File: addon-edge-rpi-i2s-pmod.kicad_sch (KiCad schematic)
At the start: 34 parts, among them J1 PMOD1, J10 Conn_01x02, J11 Conn_01x01, J2 PMOD2, J3 PMOD3, J4 Conn_01x06, J5 Conn_01x06, J6 Conn_02x04_Top_Bottom, J7 Conn_01x03, J8 Conn_01x04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

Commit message: update 10/02/22 initial autorouting
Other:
- note added: "UART FPGA / RPi"
- note removed: "UART RPi"
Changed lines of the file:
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@@
     (effects (font (size 2.54 2.54)) (justify left bottom))
   )
-  (text "UART RPi" (at 22.86 140.97 0)
+  (text "UART FPGA / RPi" (at 20.32 140.97 0)
     (effects (font (size 1.27 1.27)) (justify left bottom))
   )

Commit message: rev 0.40
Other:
- note removed: "MIDI I2S SBC Pmod Edge Interface v0.1"
- note removed: "Somhic 09/02/22"
- note removed: "design rev. 0.38"
- company: Somhic -> Created by Hard Team Deca
- title: Addon Edge mt32-Pi Multicore  -> MIDI I2S SBC Pmod Edge Interface
- moved on the sheet: BUT1, BUT2, H1, H2, H3, H4, J1, J10, J11, J2, J3, J4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

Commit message: rev. 0.41
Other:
- note added: "Central +5V"
- note added: "DOUBLE PMOD 1,2"
- note added: "PMOD 3 (SPI+UART)"
- note removed: "Double Pmod +5V"
- note removed: "PMOD 3 Multicore"
- note removed: "PMODS 1,2"
- company: Created by Hard Team Deca -> Hard Team Deca
- moved on the sheet: BUT1, BUT2, H1, H2, H3, H4, J1, J10, J11, J2, J3, J4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

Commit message: 0.42
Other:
- note added: "EXPOSAR 8 PINS SRAM I 2 PINS I2C"

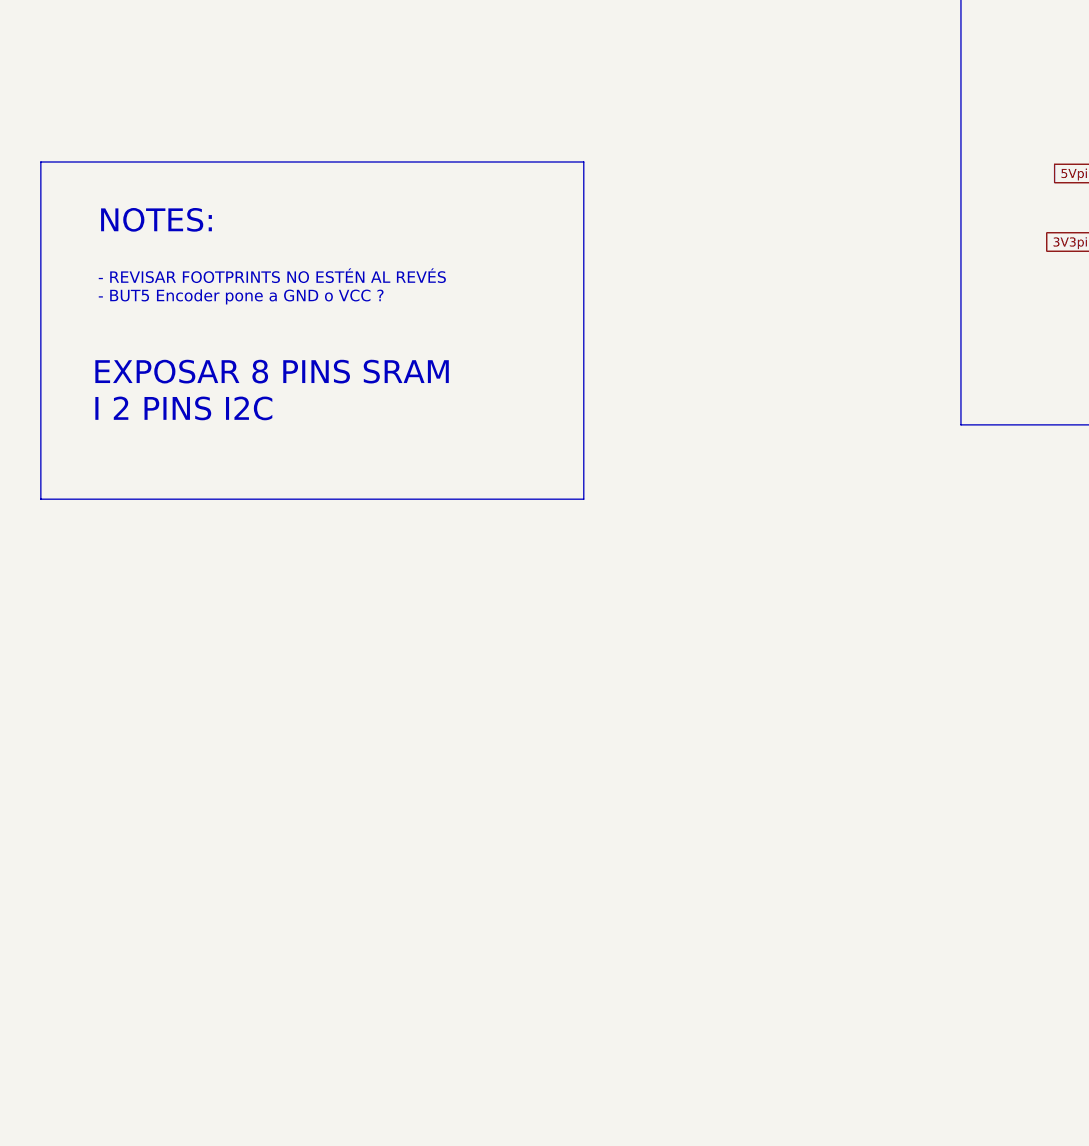
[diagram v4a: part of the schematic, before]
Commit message: modified jumper spacing for allowing switches
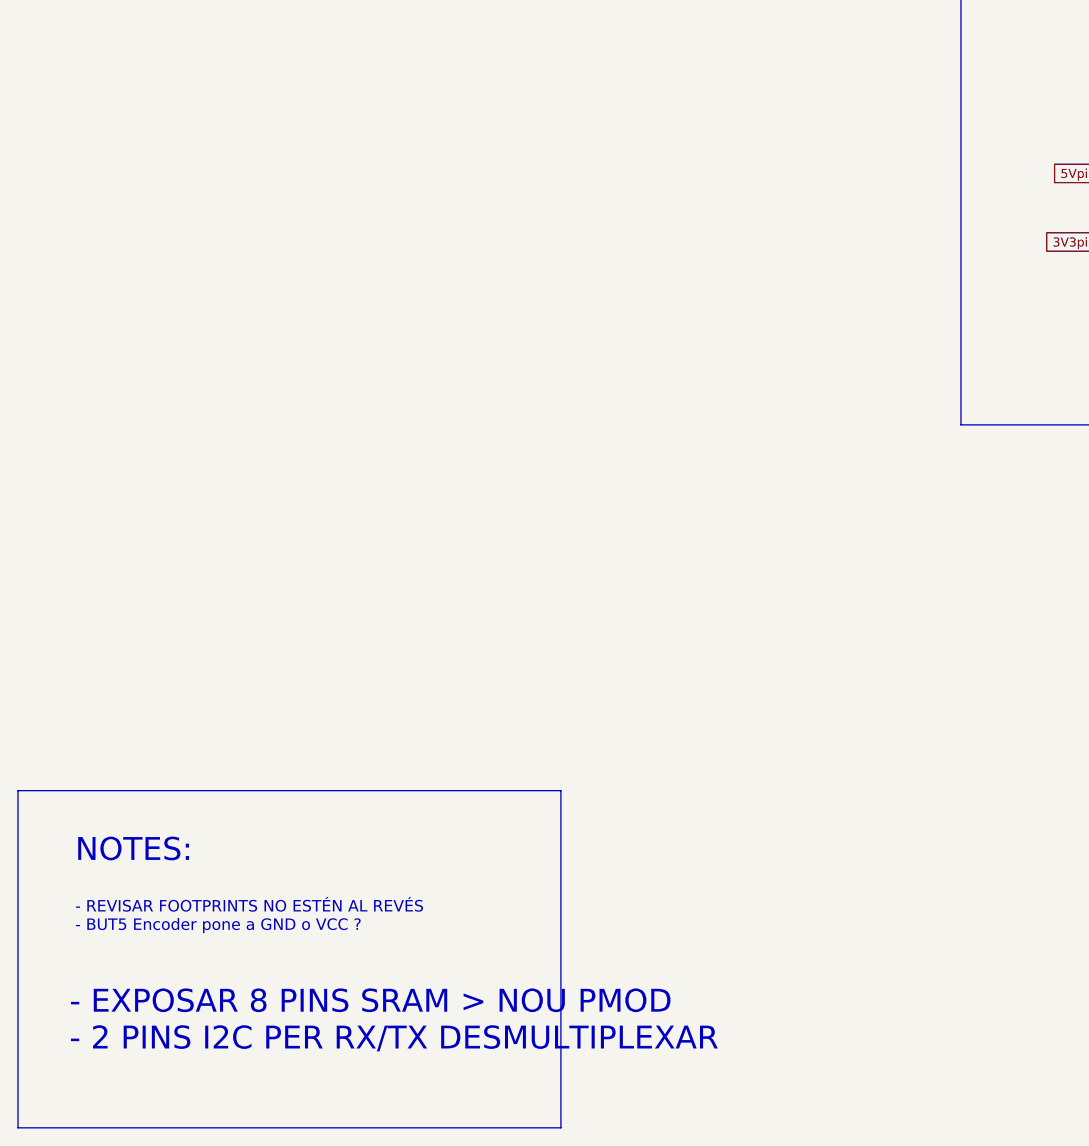
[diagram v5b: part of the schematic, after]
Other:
- note added: "- EXPOSAR 8 PINS SRAM > NOU PMOD - 2 PINS I2C PER RX/TX DESMULTIPLEXAR"
- note removed: "EXPOSAR 8 PINS SRAM I 2 PINS I2C"
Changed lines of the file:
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@@
     (stroke (width 0) (type default) (color 0 0 0 0))
   )
-  (polyline (pts (xy -3.81 253.365) (xy -64.135 253.365))
+  (polyline (pts (xy -6.35 323.215) (xy -66.675 323.215))
     (stroke (width 0) (type default) (color 0 0 0 0))
   )
@@
     (stroke (width 0) (type default) (color 0 0 0 0))
   )
-  (polyline (pts (xy -3.81 215.9) (xy -3.81 253.365))
+  (polyline (pts (xy -6.35 285.75) (xy -6.35 323.215))
     (stroke (width 0) (type default) (color 0 0 0 0))
   )
@@
     (stroke (width 0) (type default) (color 0 0 0 0))
   )
-  (polyline (pts (xy -64.135 215.9) (xy -3.81 215.9))
+  (polyline (pts (xy -66.675 285.75) (xy -6.35 285.75))
     (stroke (width 0) (type default) (color 0 0 0 0))
   )
@@
     (stroke (width 0) (type default) (color 0 0 0 0))
   )
-  (polyline (pts (xy -64.135 215.9) (xy -64.135 253.365))
+  (polyline (pts (xy -66.675 285.75) (xy -66.675 323.215))
     (stroke (width 0) (type default) (color 0 0 0 0))
   )
@@
     (effects (font (size 2.54 2.54)) (justify left bottom))
   )
-  (text "NOTES:" (at -57.785 224.155 0)
+  (text "NOTES:" (at -60.325 294.005 0)
     (effects (font (size 2.54 2.54)) (justify left bottom))
   )
@@
     (effects (font (size 1.27 1.27)) (justify left bottom))
   )
-  (text "EXPOSAR 8 PINS SRAM\nI 2 PINS I2C" (at -58.42 245.11 0)
+  (text "- EXPOSAR 8 PINS SRAM > NOU PMOD\n- 2 PINS I2C PER RX/TX DESMULTIPLEXAR"
+    (at -60.96 314.96 0)
     (effects (font (size 2.54 2.54)) (justify left bottom))
   )
@@
   )
   (text "\n\n- REVISAR FOOTPRINTS NO ESTÉN AL REVÉS\n- BUT5 Encoder pone a GND o VCC ?\n"
-    (at -57.785 231.775 0)
-    (effects (font (size 1.27 1.27)) (justify left bottom))
-  )
+    (at -60.325 301.625 0)
+    (effects (font (size 1.27 1.27)) (justify left bottom))
+  )

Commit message: v0.50 major changes
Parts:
- removed J6: Conn_02x04_Top_Bottom, Connector_PinSocket_2.54mm:PinSocket_2x04_P2.54mm_Vertical, symbol Connector_Generic:Conn_02x04_Odd_Even
- removed JP12: Conn_01x03, Connector_PinHeader_2.54mm:PinHeader_1x03_P2.54mm_Horizontal, symbol Connector_Generic:Conn_01x03
- removed JP31, JP32: Conn_01x03, Connector_PinHeader_2.54mm:PinHeader_1x03_P2.54mm_Vertical, symbol Connector_Generic:Conn_01x03
- added J12: Conn_01x02, Connector_PinSocket_2.54mm:PinSocket_2x01_P2.54mm_Horizontal, symbol Connector_Generic:Conn_01x02
- added J4: PMOD4, gomaDOSzero:PMOD_Female_Horizontal_2, symbol Connector_Generic:Conn_02x06_Top_Bottom
- added JP12: Conn_01x02, Connector_PinHeader_2.54mm:PinHeader_1x02_P2.54mm_Horizontal, symbol Connector_Generic:Conn_01x02
- added JPS1, JPS2: SolderJumper_3_Open, Jumper:SolderJumper-3_P1.3mm_Open_RoundedPad1.0x1.5mm_NumberLabels, symbol Jumper:SolderJumper_3_Open
- J8: footprint gomaDOSzero:OLED_091_DISPLAY -> gomaDOSzero:I2C_DISPLAY_MULTI2
- renumbered J11 to J13, J4 to J5, J5 to J6
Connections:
- net B16_PMOD2_D3 is gone; now on net A25_PMOD2_D3: J2.4 (Pin_4)
- net B16_PMOD_UARTX_MIDI is gone; now on net B16_UART_TX_MIDI: EDGE1.B16 (/MREQ)
- net B1_CE2_UART_RX is gone; now on net B1_UART_RX: EDGE1.B1 (A15)
- net +5V: now also J12.1 (Pin_1)
- net 3V3pi: now also JPS1.3 (B), JPS2.3 (B); no longer J8.2 (Pin_2)
- net GND: now also J12.2 (Pin_2), J4.11 (Pin_11), J4.5 (Pin_5), JPS1.1 (A), JPS2.1 (A); no longer J8.1 (Pin_1)
- net JP11_Vout: now also JP12.1 (Pin_1)
- net VIN: now also JP12.2 (Pin_2)
- net B10_SRAMDQ13: now reaches EDGE1.B10 (D5)
- net B10_SRAMDQ13: now also J4.8 (Pin_8)
- net B11_SRAMDQ11: now reaches EDGE1.B11 (D3)
- net B11_SRAMDQ11: now also J4.4 (Pin_4)
- net B12_SRAMDQ12: now reaches EDGE1.B12 (D4)
- net B12_SRAMDQ12: now also J4.7 (Pin_7)
- net B15_SCL_PM1_D2: now reaches EDGE1.B15 (/HALT)
- net B15_SCL_PM1_D2: now also J1.3 (Pin_3)
- net B21_SDA_PM1_D3: now reaches EDGE1.B21 (/WAIT)
- net B21_SDA_PM1_D3: now also J1.4 (Pin_4)
- net B3_SRAMDQ15: now reaches EDGE1.B3 (D7)
- net B3_SRAMDQ15: now also J4.10 (Pin_10)
- net B6_SRAMDQ8: now reaches EDGE1.B6 (D0)
- net B6_SRAMDQ8: now also J4.1 (Pin_1)
- net B7_SRAMDQ9: now reaches EDGE1.B7 (D1)
- net B7_SRAMDQ9: now also J4.2 (Pin_2)
- net B8_SRAMDQ10: now reaches EDGE1.B8 (D2)
- net B8_SRAMDQ10: now also J4.3 (Pin_3)
- net B9_SRAMDQ14: now reaches EDGE1.B9 (D6)
- net B9_SRAMDQ14: now also J4.9 (Pin_9)
- net VH_PMOD: now reaches J3.12 (Pin_12), J3.6 (Pin_6), JP5.2 (Pin_2)
- net VH_PMOD: now also J4.12 (Pin_12), J4.6 (Pin_6)
- net A12_PMOD1_D2 renamed A12_PMOD1_D6
- net A12_PMOD1_D6: now also J1.9 (Pin_9); no longer J1.3 (Pin_3)
- net A20_PMOD2_D4 renamed A20_PMOD2_D5
- net A20_PMOD2_D5: now also J2.8 (Pin_8); no longer J2.7 (Pin_7)
- net A21_PMOD2_D0 renamed A21_PMOD2_D1
- net A21_PMOD2_D1: now also J2.2 (Pin_2); no longer J2.1 (Pin_1)
- net A22_PMOD2_D1 renamed A22_PMOD2_D6
- net A22_PMOD2_D6: now also J2.9 (Pin_9); no longer J2.2 (Pin_2)
- net A23_PMOD2_D5 renamed A23_PMOD2_D2
- net A23_PMOD2_D2: now also J2.3 (Pin_3); no longer J2.8 (Pin_8)
- net A24_PMOD2_D2 renamed A24_PMOD2_D7
- net A24_PMOD2_D7: now also J2.10 (Pin_10); no longer J2.3 (Pin_3)
- net A25_PMOD2_D6 renamed A25_PMOD2_D3
- net A25_PMOD2_D3: no longer J2.9 (Pin_9)
- net B17_PMOD1_D6 renamed B17_PMOD1_D7
- net B17_PMOD1_D7: now also J1.10 (Pin_10); no longer J1.9 (Pin_9)
- net B18_PMOD1_D3 renamed B18_PMOD2_D4
- net B18_PMOD2_D4: now also J2.7 (Pin_7); no longer J1.4 (Pin_4)
- net B19_PMOD1_D7 renamed B19_PMOD2_D0
- net B19_PMOD2_D0: now also J2.1 (Pin_1); no longer J1.10 (Pin_10)
- net B1_SPI1_CE2 renamed B27_SPI1CE2
- net B27_SPI1CE2: now also EDGE1.B27 (A10)
- removed net B27_PMOD2_D7: EDGE1.B27 (A10), J2.10 (Pin_10)
- new net DISPLAY_PS1: J8.1 (Pin_1), JPS1.2 (C)
- new net DISPLAY_PS2: J8.2 (Pin_2), JPS2.2 (C)
- no-connect marks 32 -> 22
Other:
- note added: "- REVISAR FOOTPRINTS NO ESTIGUIN AL REVÉS"
- note added: "BUTTONS"
- note added: "JUMPERS VCC/GND DISPLAY"
- note added: "PMOD 1 (I2C)"
- note added: "PMOD 2"
- note added: "PMOD 4 (SRAM)"
- note added: "UART"
- note removed: "(FPGA)"
- note removed: "- EXPOSAR 8 PINS SRAM > NOU PMOD - 2 PINS I2C PER RX/TX DESMULTIPLEXAR"
- note removed: "- REVISAR FOOTPRINTS NO ESTÉN AL REVÉS - BUT5 Encoder pone a GND o VCC ?"
- note removed: "DOUBLE PMOD 1,2"
- note removed: "HEADERS Raspberry Pi"
- note removed: "JUMPERS 3 OTHERS/UART"
- note removed: "PMOD2_D06 / UART TX"
- note removed: "POWER RPi"
- note removed: "SPI1 CE2 / UART RX"
- moved on the sheet: BUT1, BUT2, H1, H2, H3, H4, J1, J10, J13, J2, J3, J5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

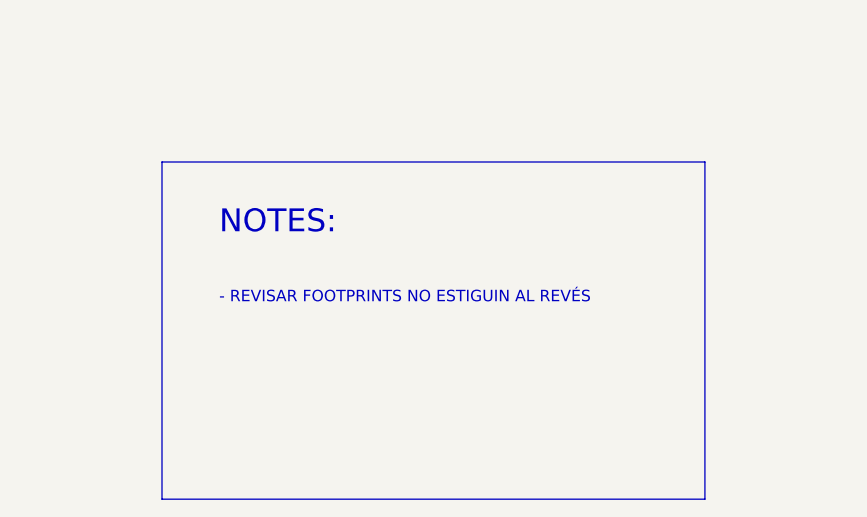
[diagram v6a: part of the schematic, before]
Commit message: v0.52 changed tracks pmod 1 & 2
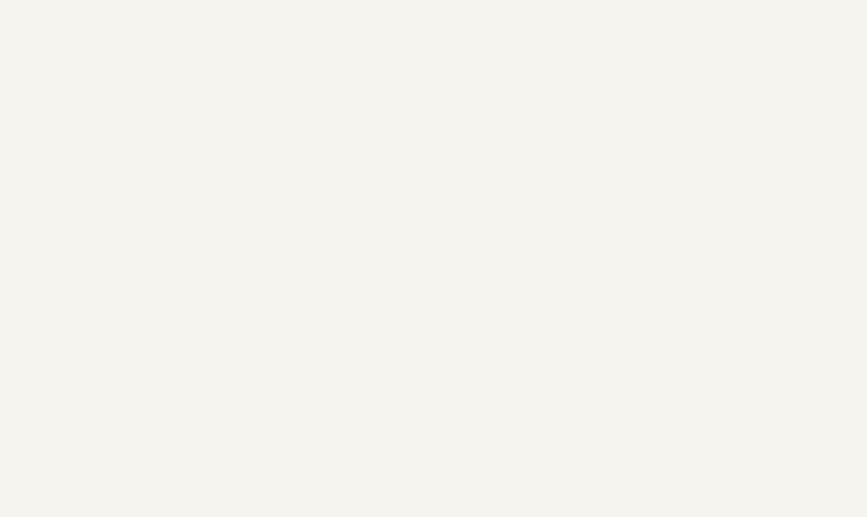
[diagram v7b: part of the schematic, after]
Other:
- note removed: "- REVISAR FOOTPRINTS NO ESTIGUIN AL REVÉS"
- note removed: "NOTES:"
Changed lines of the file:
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@@
-    (stroke (width 0) (type default) (color 0 0 0 0))
-  )
-  (polyline (pts (xy 247.65 340.995) (xy 187.325 340.995))
     (stroke (width 0) (type default) (color 0 0 0 0))
   )
@@
     (stroke (width 0) (type default) (color 0 0 0 0))
   )
-  (polyline (pts (xy 247.65 303.53) (xy 247.65 340.995))
-    (stroke (width 0) (type default) (color 0 0 0 0))
-  )
   (wire (pts (xy 167.005 175.895) (xy 189.865 175.895))
     (stroke (width 0) (type default) (color 0 0 0 0))
@@
     (stroke (width 0) (type default) (color 0 0 0 0))
   )
-  (polyline (pts (xy 187.325 303.53) (xy 247.65 303.53))
-    (stroke (width 0) (type default) (color 0 0 0 0))
-  )
   (wire (pts (xy 249.555 81.28) (xy 276.225 81.28))
     (stroke (width 0) (type default) (color 0 0 0 0))
@@
     (stroke (width 0) (type default) (color 0 0 0 0))
   )
-  (polyline (pts (xy 187.325 303.53) (xy 187.325 340.995))
-    (stroke (width 0) (type default) (color 0 0 0 0))
-  )
   (wire (pts (xy 88.265 136.525) (xy 83.185 136.525))
     (stroke (width 0) (type default) (color 0 0 0 0))
@@
     (effects (font (size 2.54 2.54)) (justify left bottom))
   )
-  (text "NOTES:" (at 193.675 311.785 0)
-    (effects (font (size 2.54 2.54)) (justify left bottom))
-  )
   (text "(mt32-Pi)" (at 238.125 81.28 0)
     (effects (font (size 1.27 1.27)) (justify left bottom))
@@
     (effects (font (size 1.27 1.27)) (justify left bottom))
   )
-  (text "\n\n- REVISAR FOOTPRINTS NO ESTIGUIN AL REVÉS\n" (at 193.675 319.405 0)
-    (effects (font (size 1.27 1.27)) (justify left bottom))
-  )

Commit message: comments on schematic
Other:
- note added: "(FPGA Edge)"
- note added: "(RPI)"
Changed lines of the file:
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@@
     (effects (font (size 2.54 2.54)) (justify left bottom))
+  )
+  (text "(RPI)" (at 298.45 131.445 0)
+    (effects (font (size 1.27 1.27)) (justify left bottom))
   )
   (text "JUMPERS 2 I2S SOURCE" (at 273.685 102.87 0)
@@
   (text "EDGE" (at 182.245 31.115 0)
     (effects (font (size 2.54 2.54)) (justify left bottom))
+  )
+  (text "(FPGA Edge)" (at 298.45 165.1 0)
+    (effects (font (size 1.27 1.27)) (justify left bottom))
   )
   (text "(Edge)" (at 44.45 149.225 0)
@@
     (effects (font (size 1.27 1.27)) (justify left bottom))
   )
+  (text "(RPI)" (at 298.45 153.035 0)
+    (effects (font (size 1.27 1.27)) (justify left bottom))
+  )
   (text "(mt32-Pi)" (at 342.265 55.88 0)
     (effects (font (size 1.27 1.27)) (justify left bottom))
@@
   )
   (text "(RPi)" (at 227.965 127.635 0)
+    (effects (font (size 1.27 1.27)) (justify left bottom))
+  )
+  (text "(FPGA Edge)" (at 298.45 143.51 0)
+    (effects (font (size 1.27 1.27)) (justify left bottom))
+  )
+  (text "(FPGA Edge)" (at 298.45 123.19 0)
     (effects (font (size 1.27 1.27)) (justify left bottom))
   )
@@
     (effects (font (size 1.27 1.27)) (justify left bottom))
   )
+  (text "(RPI)" (at 298.45 111.125 0)
+    (effects (font (size 1.27 1.27)) (justify left bottom))
+  )
